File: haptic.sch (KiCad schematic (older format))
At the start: 6 parts, among them M2401 Motor, Q2401 DMG2301L

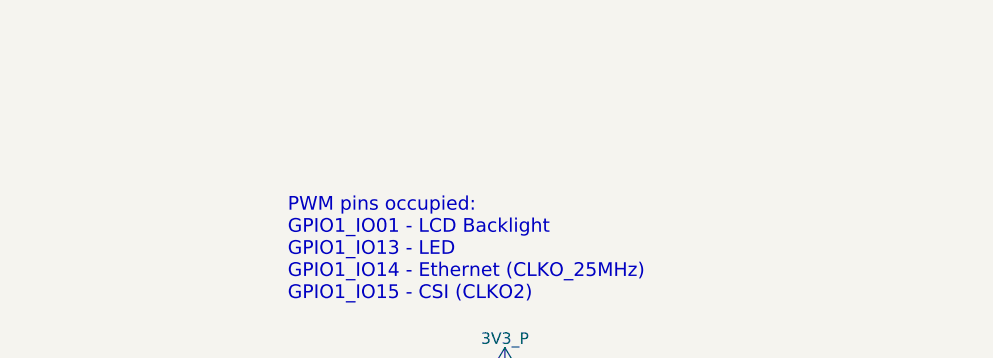
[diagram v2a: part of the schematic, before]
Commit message: Move more symbols, sheets, and pins around on the front sheet to make it even clearer, bring back the old hierarchical structure (again), bring back each sheet's title, add large text "titles" to each sheet reflecting what they are for
Still need to double check everything on the first page.
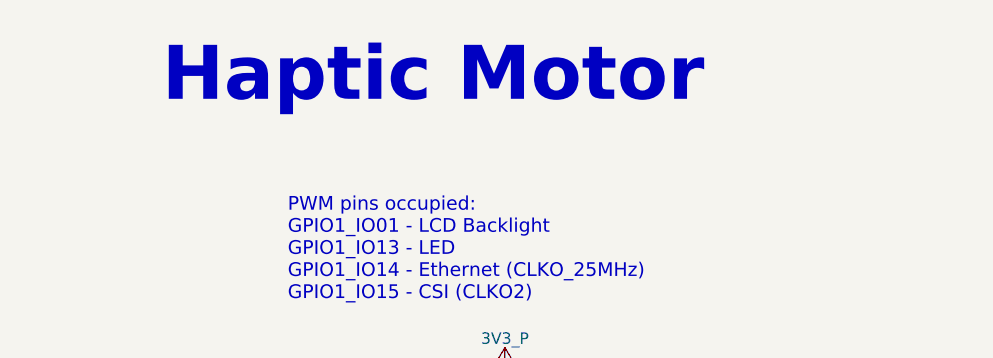
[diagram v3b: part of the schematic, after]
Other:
- note added: "Haptic Motor"
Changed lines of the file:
@@
 encoding utf-8
 Sheet 24 24
-Title "Librem5 development kit"
+Title "Haptic/Vibration Motor"
 Date "2018-06-11"
 Rev "v0.1.0"
@@
 $EndDescr
 $Comp
-L GND #PWR0265
+L GND #PWR0376
 U 1 1 5AFCF90B
 P 6050 4300
-F 0 "#PWR0265" H 6050 4050 50  0001 C CNN
+F 0 "#PWR0376" H 6050 4050 50  0001 C CNN
 F 1 "GND" H 6050 4150 50  0000 C CNN
 F 2 "" H 6050 4300 50  0001 C CNN
@@
 $EndComp
 $Comp
-L 3V3_P #PWR0266
+L 3V3_P #PWR0377
 U 1 1 5AFD13E2
 P 6050 2950
-F 0 "#PWR0266" H 6050 2800 50  0001 C CNN
+F 0 "#PWR0377" H 6050 2800 50  0001 C CNN
 F 1 "3V3_P" H 6050 3090 50  0000 C CNN
 F 2 "" H 6050 2950 50  0001 C CNN
@@
 	-1   0    0    1
 $EndComp
+Text Notes 4550 1800 0    236  ~ 47
+Haptic Motor
 $EndSCHEMATC

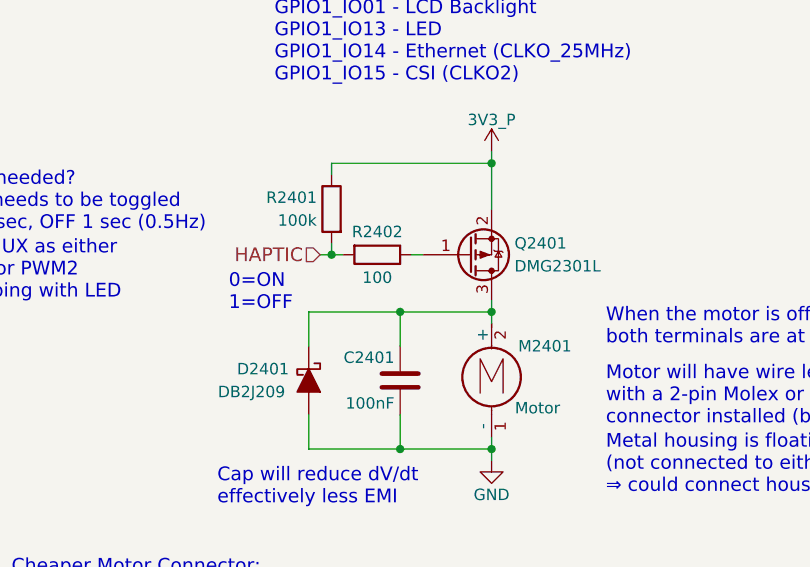
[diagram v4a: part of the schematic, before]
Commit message: Add AC coupling caps to the HDMI_AUXP/N diff pair which were mistakenly left out, fix a couple typos/errors that were made when transitioning to the new top-leve sheet, make the M.2s' I2C RX TX hierarchical signals consistent and clearer
Hopefully all lingering errors have been caught, this will likely be the schematic commit that gets reviewed (fingers crossed).
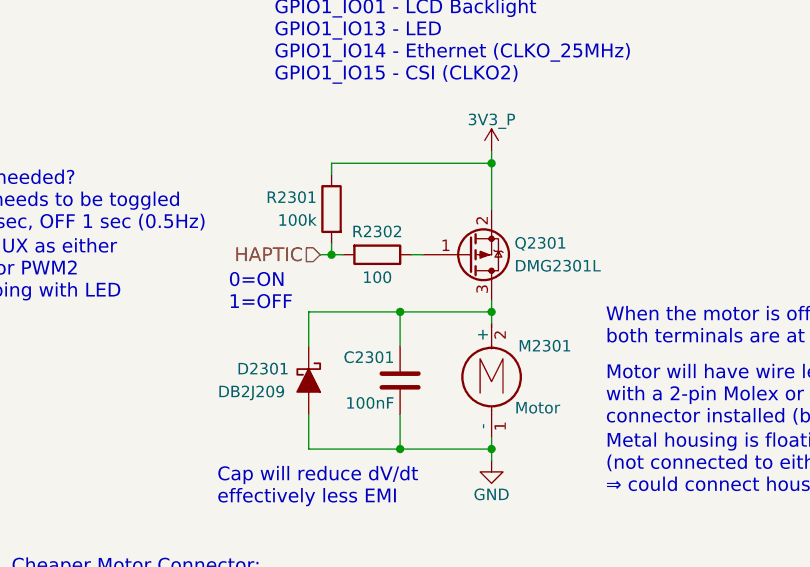
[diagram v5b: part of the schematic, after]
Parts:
- renumbered C2401 to C2301, D2401 to D2301, M2401 to M2301, Q2401 to Q2301, R2401 to R2301, R2402 to R2302
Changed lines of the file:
@@
 $Descr A4 11693 8268
 encoding utf-8
-Sheet 24 24
+Sheet 23 24
 Title "Haptic/Vibration Motor"
 Date "2018-06-14"
@@
 $EndDescr
 $Comp
-L GND #PWR2402
+L GND #PWR0349
 U 1 1 5AFCF90B
 P 6050 4300
-F 0 "#PWR2402" H 6050 4050 50  0001 C CNN
+F 0 "#PWR0349" H 6050 4050 50  0001 C CNN
 F 1 "GND" H 6050 4150 50  0000 C CNN
 F 2 "" H 6050 4300 50  0001 C CNN
@@
 When the motor is off\nboth terminals are at GND
 $Comp
-L Q_PMOS_GSD Q2401
+L Q_PMOS_GSD Q2301
 U 1 1 5AFD137F
 P 5950 3400
-F 0 "Q2401" H 6150 3350 50  0000 L CNN
+F 0 "Q2301" H 6150 3350 50  0000 L CNN
 F 1 "DMG2301L" H 6150 3450 50  0000 L CNN
 F 2 "TO_SOT_Packages_SMD:SOT-23" H 6150 3500 50  0001 C CNN
@@
 $EndComp
 $Comp
-L 3V3_P #PWR2401
+L 3V3_P #PWR0350
 U 1 1 5AFD13E2
 P 6050 2950
-F 0 "#PWR2401" H 6050 2800 50  0001 C CNN
+F 0 "#PWR0350" H 6050 2800 50  0001 C CNN
 F 1 "3V3_P" H 6050 3090 50  0000 C CNN
 F 2 "" H 6050 2950 50  0001 C CNN
@@
 $EndComp
 $Comp
-L R R2401
+L R R2301
 U 1 1 5AFD2E14
 P 5350 3200
-F 0 "R2401" H 5525 3250 50  0000 C CNN
+F 0 "R2301" H 5525 3250 50  0000 C CNN
 F 1 "100k" H 5500 3150 50  0000 C CNN
 F 2 "Resistors_SMD:R_0603" V 5280 3200 50  0001 C CNN
@@
 HAPTIC
 $Comp
-L D_Schottky_ALT D2401
+L D_Schottky_ALT D2301
 U 1 1 5AFD563E
 P 5250 3950
-F 0 "D2401" V 5200 3750 50  0000 C CNN
+F 0 "D2301" V 5200 3750 50  0000 C CNN
 F 1 "DB2J209" V 5300 3700 50  0000 C CNN
 F 2 "dvk-mx8m-bsb:SMini2-F5-B" H 5250 3950 50  0001 C CNN
@@
 $EndComp
 $Comp
-L R R2402
+L R R2302
 U 1 1 5AFFD30C
 P 5550 3400
-F 0 "R2402" V 5450 3400 50  0000 C CNN
+F 0 "R2302" V 5450 3400 50  0000 C CNN
 F 1 "100" V 5650 3400 50  0000 C CNN
 F 2 "Resistors_SMD:R_0603" V 5480 3400 50  0001 C CNN
@@
 $EndComp
 $Comp
-L C C2401
+L C C2301
 U 1 1 5B0285ED
 P 5650 3950
-F 0 "C2401" H 5675 4050 50  0000 L CNN
+F 0 "C2301" H 5675 4050 50  0000 L CNN
 F 1 "100nF" H 5675 3850 50  0000 L CNN
 F 2 "Capacitors_SMD:C_0603" H 5688 3800 50  0001 C CNN
@@
 Metal housing is floating\n(not connected to either pin)\n⇒ could connect housing to GND
 $Comp
-L Motor_Haptic M2401
+L Motor_Haptic M2301
 U 1 1 5B40BABE
 P 6050 4000
-F 0 "M2401" H 5700 3800 50  0000 L CNN
+F 0 "M2301" H 5700 3800 50  0000 L CNN
 F 1 "Motor" H 5750 4100 50  0000 L TNN
 F 2 "dvk-mx8m-bsb:BY0820Z021L20" H 6050 3965 50  0001 C CNN

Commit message: Move the WLAN+BT M.2 sheet back to page 18 rather than the last page (24)
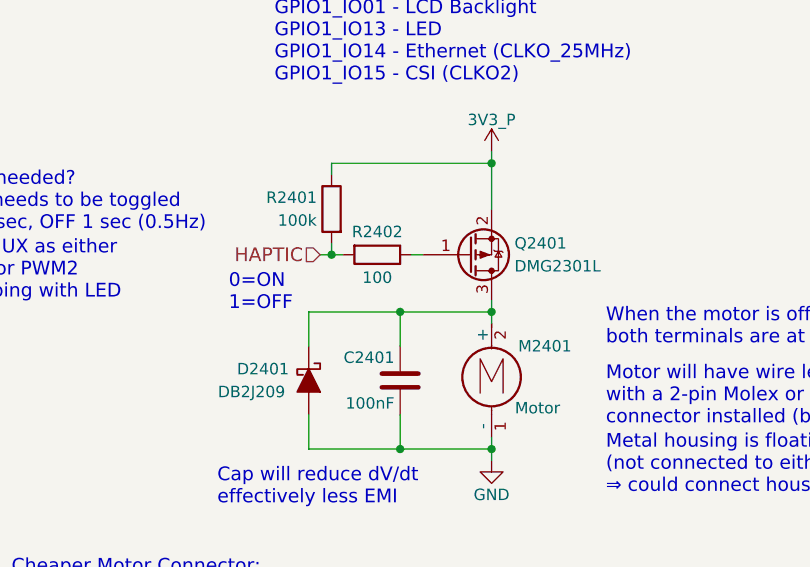
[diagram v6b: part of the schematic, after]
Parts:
- renumbered C2301 to C2401, D2301 to D2401, M2301 to M2401, Q2301 to Q2401, R2301 to R2401, R2302 to R2402
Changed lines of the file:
@@
 $Descr A4 11693 8268
 encoding utf-8
-Sheet 23 24
+Sheet 24 24
 Title "Haptic/Vibration Motor"
-Date "2018-06-14"
+Date "2018-06-15"
 Rev "v0.1.0"
 Comp "Copyright 2018 GNU GPLv3"
@@
 $EndDescr
 $Comp
-L GND #PWR0349
+L GND #PWR0375
 U 1 1 5AFCF90B
 P 6050 4300
-F 0 "#PWR0349" H 6050 4050 50  0001 C CNN
+F 0 "#PWR0375" H 6050 4050 50  0001 C CNN
 F 1 "GND" H 6050 4150 50  0000 C CNN
 F 2 "" H 6050 4300 50  0001 C CNN
@@
 When the motor is off\nboth terminals are at GND
 $Comp
-L Q_PMOS_GSD Q2301
+L Q_PMOS_GSD Q2401
 U 1 1 5AFD137F
 P 5950 3400
-F 0 "Q2301" H 6150 3350 50  0000 L CNN
+F 0 "Q2401" H 6150 3350 50  0000 L CNN
 F 1 "DMG2301L" H 6150 3450 50  0000 L CNN
 F 2 "TO_SOT_Packages_SMD:SOT-23" H 6150 3500 50  0001 C CNN
@@
 $EndComp
 $Comp
-L 3V3_P #PWR0350
+L 3V3_P #PWR0376
 U 1 1 5AFD13E2
 P 6050 2950
-F 0 "#PWR0350" H 6050 2800 50  0001 C CNN
+F 0 "#PWR0376" H 6050 2800 50  0001 C CNN
 F 1 "3V3_P" H 6050 3090 50  0000 C CNN
 F 2 "" H 6050 2950 50  0001 C CNN
@@
 $EndComp
 $Comp
-L R R2301
+L R R2401
 U 1 1 5AFD2E14
 P 5350 3200
-F 0 "R2301" H 5525 3250 50  0000 C CNN
+F 0 "R2401" H 5525 3250 50  0000 C CNN
 F 1 "100k" H 5500 3150 50  0000 C CNN
 F 2 "Resistors_SMD:R_0603" V 5280 3200 50  0001 C CNN
@@
 HAPTIC
 $Comp
-L D_Schottky_ALT D2301
+L D_Schottky_ALT D2401
 U 1 1 5AFD563E
 P 5250 3950
-F 0 "D2301" V 5200 3750 50  0000 C CNN
+F 0 "D2401" V 5200 3750 50  0000 C CNN
 F 1 "DB2J209" V 5300 3700 50  0000 C CNN
 F 2 "dvk-mx8m-bsb:SMini2-F5-B" H 5250 3950 50  0001 C CNN
@@
 $EndComp
 $Comp
-L R R2302
+L R R2402
 U 1 1 5AFFD30C
 P 5550 3400
-F 0 "R2302" V 5450 3400 50  0000 C CNN
+F 0 "R2402" V 5450 3400 50  0000 C CNN
 F 1 "100" V 5650 3400 50  0000 C CNN
 F 2 "Resistors_SMD:R_0603" V 5480 3400 50  0001 C CNN
@@
 $EndComp
 $Comp
-L C C2301
+L C C2401
 U 1 1 5B0285ED
 P 5650 3950
-F 0 "C2301" H 5675 4050 50  0000 L CNN
+F 0 "C2401" H 5675 4050 50  0000 L CNN
 F 1 "100nF" H 5675 3850 50  0000 L CNN
 F 2 "Capacitors_SMD:C_0603" H 5688 3800 50  0001 C CNN
@@
 Metal housing is floating\n(not connected to either pin)\n⇒ could connect housing to GND
 $Comp
-L Motor_Haptic M2301
+L Motor_Haptic M2401
 U 1 1 5B40BABE
 P 6050 4000
-F 0 "M2301" H 5700 3800 50  0000 L CNN
+F 0 "M2401" H 5700 3800 50  0000 L CNN
 F 1 "Motor" H 5750 4100 50  0000 L TNN
 F 2 "dvk-mx8m-bsb:BY0820Z021L20" H 6050 3965 50  0001 C CNN
